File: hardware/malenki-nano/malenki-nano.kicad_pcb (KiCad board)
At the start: 2 copper layers, 25.4 x 23.6 mm, 20 parts, among them J1 Conn_01x02_Male, J2 Conn_01x04_Male, J5 Conn_01x02_Male, J6 Conn_01x02_Male, J7 Conn_01x02_Male, U1 A7105-MODULE, U2 generic-ldo, U3 ATtiny1614, U5 RZ7899, U6 RZ7899, U7 RZ7899

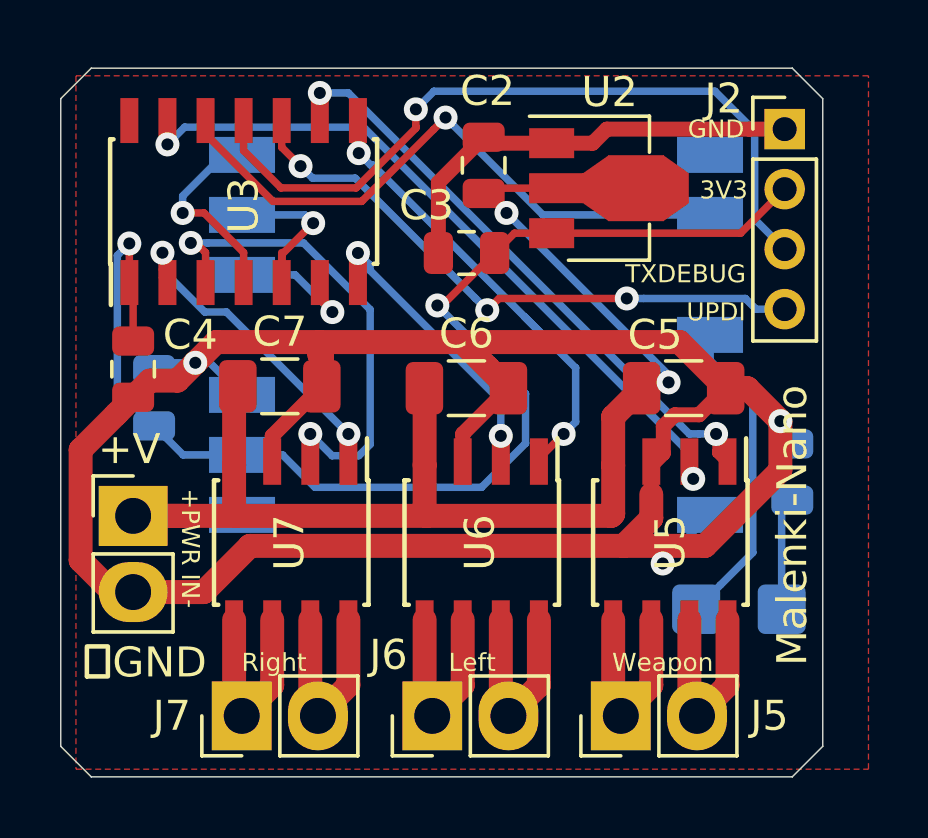
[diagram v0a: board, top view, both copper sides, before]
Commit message: Add another LED attached to TXDEBUG
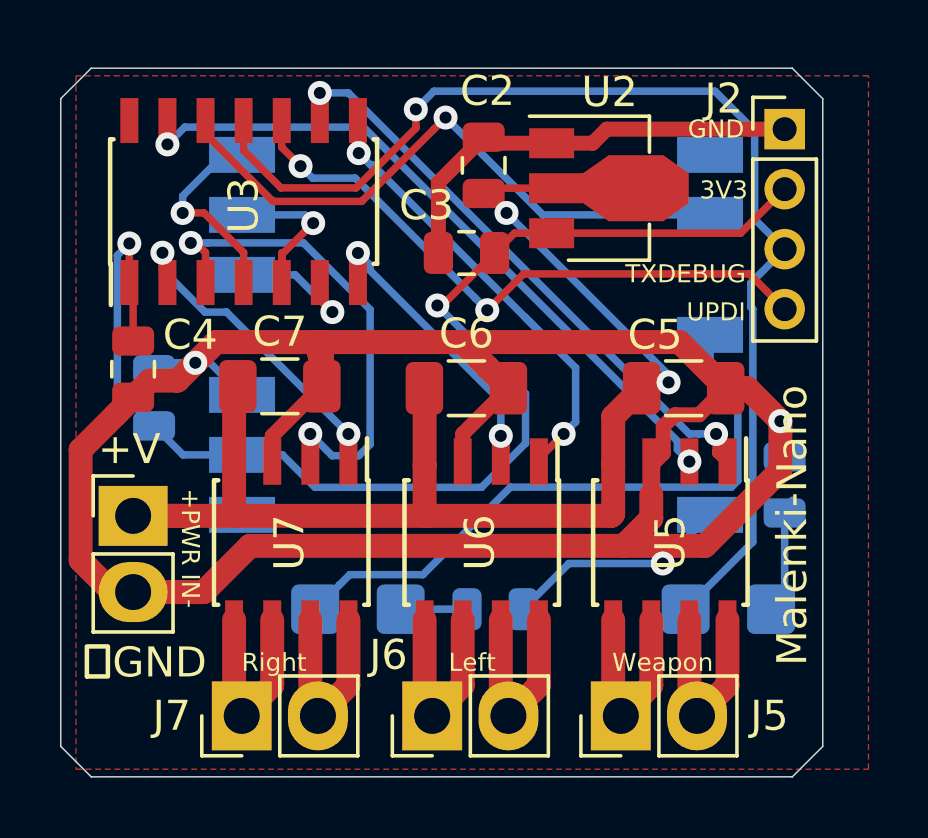
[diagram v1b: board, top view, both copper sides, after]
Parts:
- added D2: LED Red, LED_SMD:LED_1206_3216Metric_Castellated, B.Cu at (193.4, 137.4)
- added R2: 220R, Resistor_SMD:R_0805_2012Metric, B.Cu at (195.3, 133.3)
- moved D1 12.7 mm to (181.1, 137.4)
- moved R1 10.9 mm to (185.7, 137.4), turned to 0 degrees
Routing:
- net TXDEBUG: track 25.2 -> 38.6 mm
- net BLINKY: track 10.5 -> 21.1 mm
- net GND: track 96.1 -> 101.7 mm
- net Net-(D2-Pad1): track 0.00 -> 3.89 mm
- net Net-(D1-Pad1): track 3.78 -> 2.21 mm
- net MOTOR1F: track 24.4 -> 23.3 mm
- net UPDI: track 20.7 -> 21.4 mm, vias 3 -> 2
